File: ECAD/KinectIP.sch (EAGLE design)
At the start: 12 parts, among them P5+ 2PIN-FEMALE-HEADER

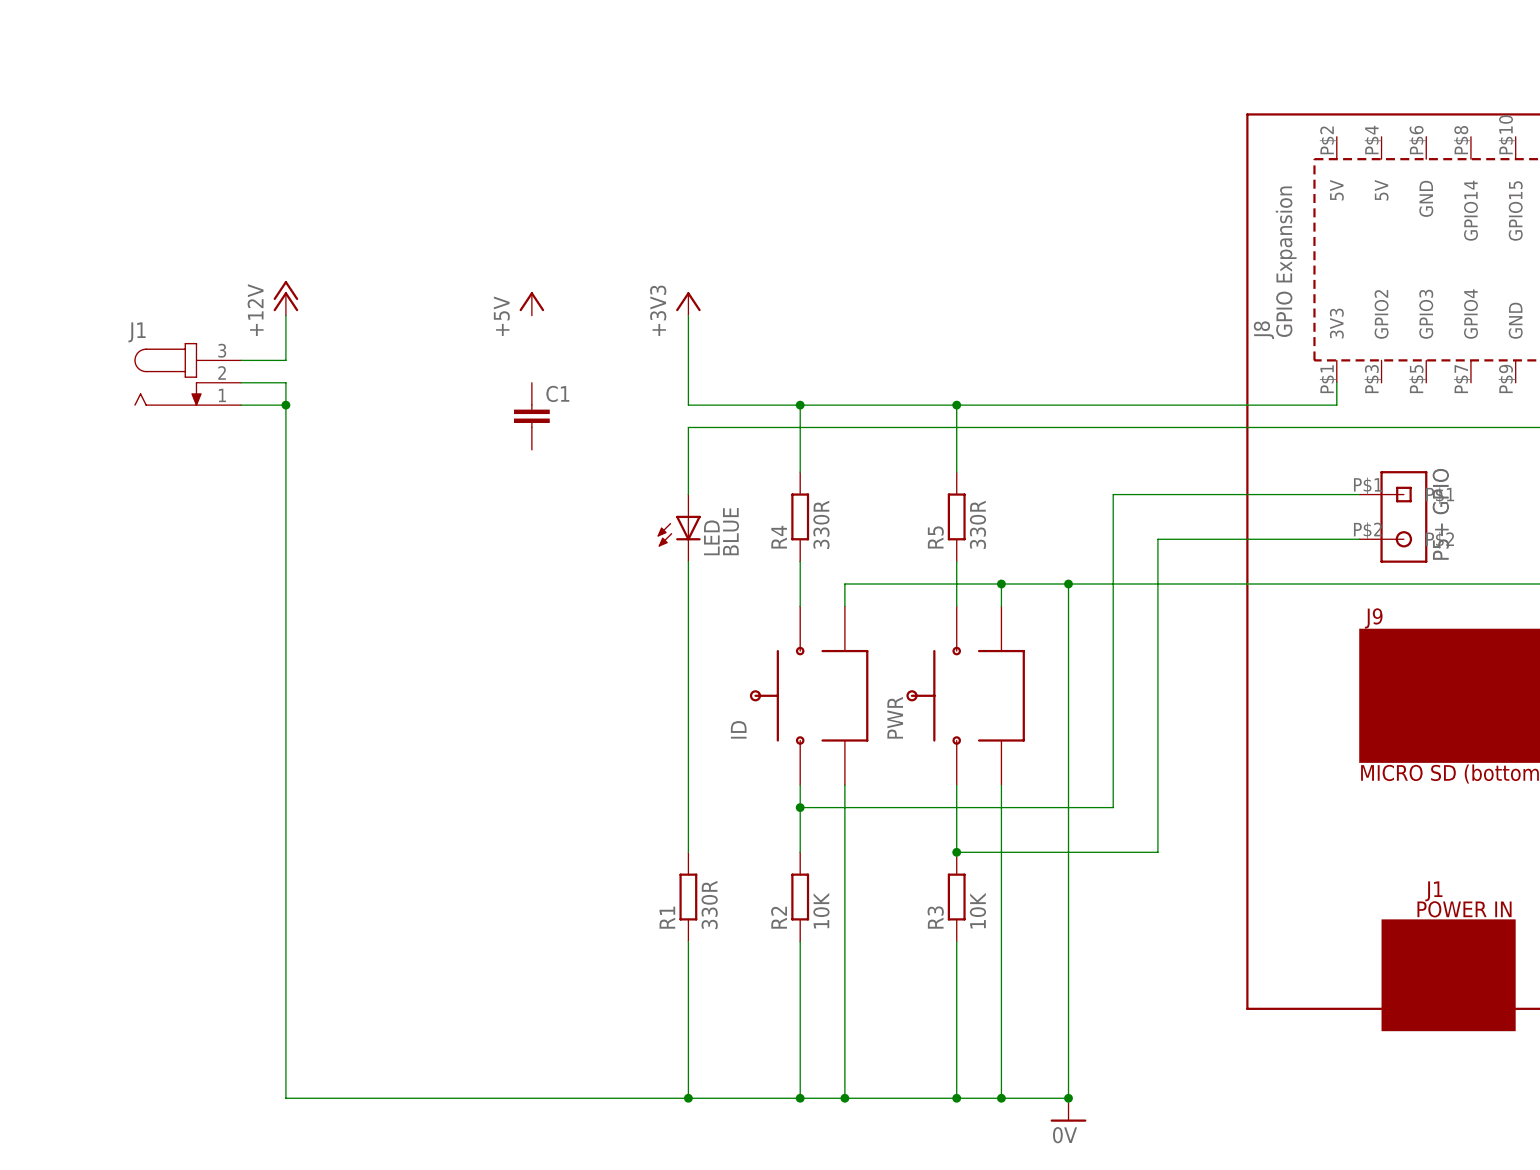
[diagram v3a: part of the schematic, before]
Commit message: add MP1584
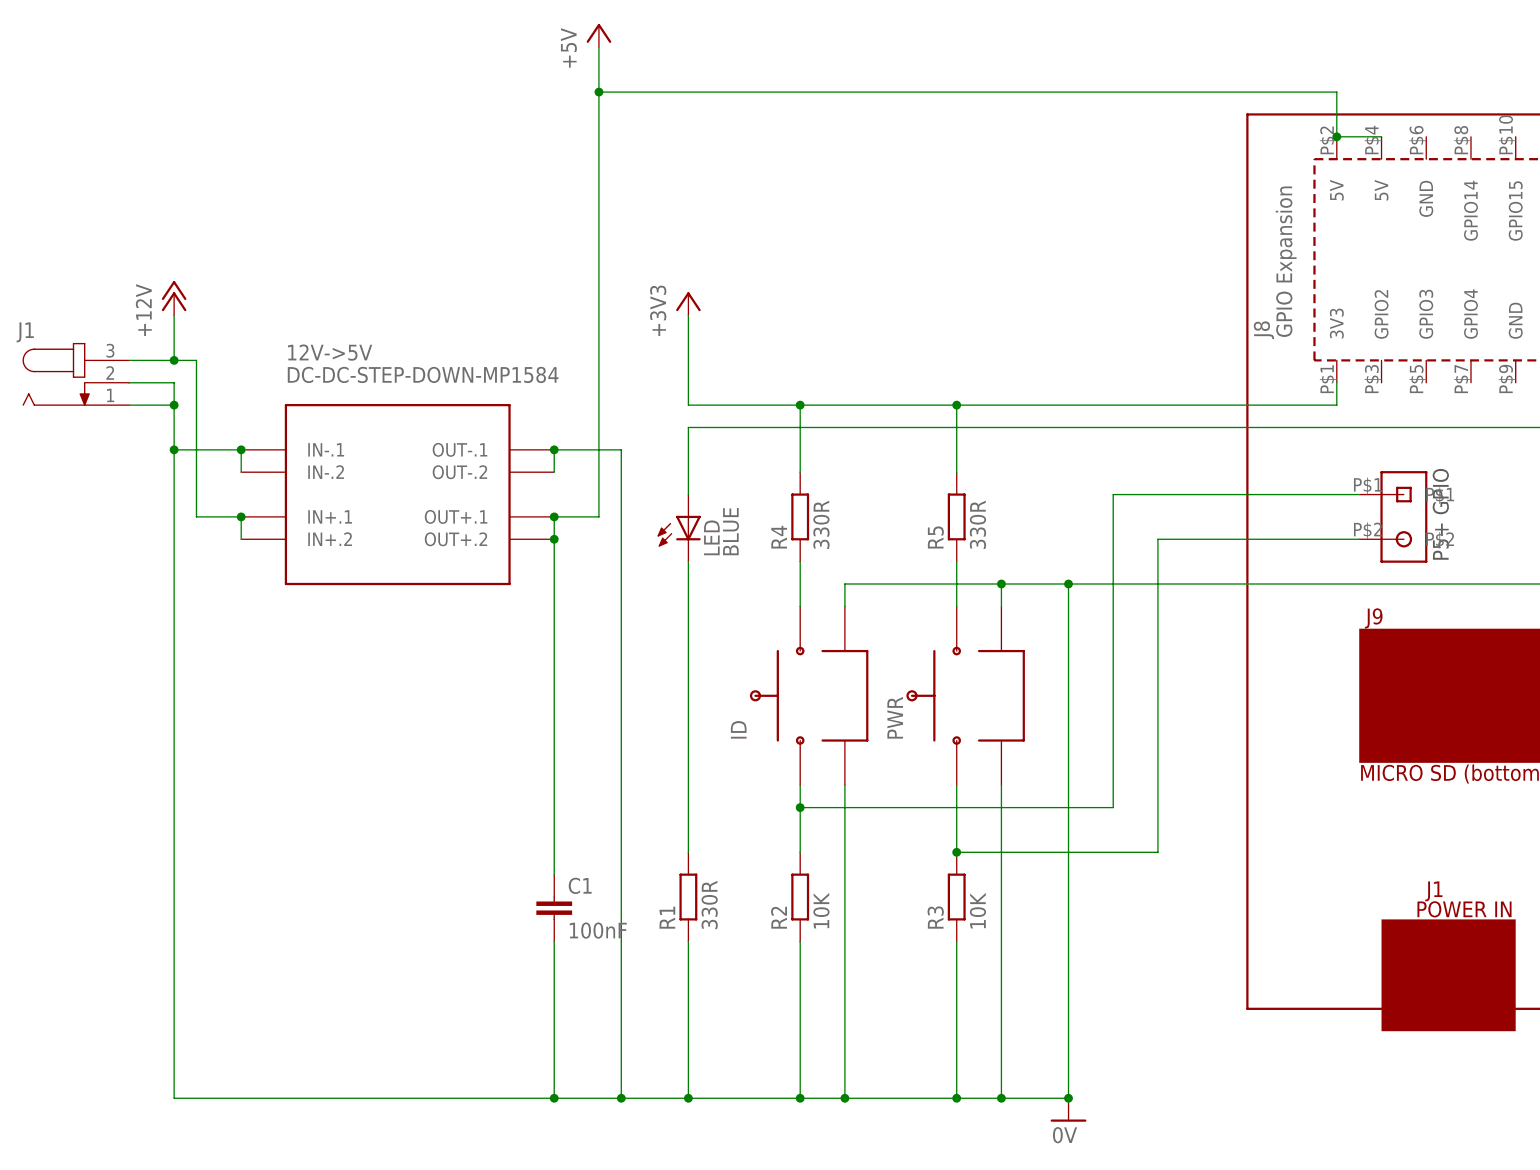
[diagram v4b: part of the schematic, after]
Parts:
- added 12V->5V: DC-DC-STEP-DOWN-MP1584, diy-modules:DC-DC-STEP-DOWN-MP1584
- C1: value (none) -> 100nF
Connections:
- new net +5V: 12V->5V.OUT+.1, 12V->5V.OUT+.2, C1.1, PCB2.5V@2, PCB2.5V@4
- net +12V: now also 12V->5V.IN+.1, 12V->5V.IN+.2
- net 0V: now also 12V->5V.IN-.1, 12V->5V.IN-.2, 12V->5V.OUT-.1, 12V->5V.OUT-.2, C1.2
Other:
- moved on the sheet: C1, J1
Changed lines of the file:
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@@
 <part name="J1" library="con-jack-3D" library_urn="urn:adsk.eagle:library:12345140" deviceset="JACK-PLUG-SLOTTED" device="0" package3d_urn="urn:adsk.eagle:package:12345148/2"/>
 <part name="LED" library="LED-90-Degree" library_urn="urn:adsk.eagle:library:12346089" deviceset="LED-90-DEG" device="" package3d_urn="urn:adsk.eagle:package:12346092/4" value="BLUE"/>
-<part name="C1" library="rcl" library_urn="urn:adsk.eagle:library:334" deviceset="C-EU" device="C0805K" package3d_urn="urn:adsk.eagle:package:23681/2"/>
+<part name="C1" library="rcl" library_urn="urn:adsk.eagle:library:334" deviceset="C-EU" device="C0805K" package3d_urn="urn:adsk.eagle:package:23681/2" value="100nF"/>
+<part name="12V-&gt;5V" library="diy-modules" library_urn="urn:adsk.eagle:library:12361804" deviceset="DC-DC-STEP-DOWN-MP1584" device="" package3d_urn="urn:adsk.eagle:package:12362133/2"/>
 </parts>
 <sheets>
@@
 <attribute name="VALUE" x="175.895" y="66.04" size="1.778" layer="96"/>
 </instance>
-<instance part="P+1" gate="1" x="116.84" y="162.56" smashed="yes">
-<attribute name="VALUE" x="114.3" y="157.48" size="1.778" layer="96" rot="R90"/>
-</instance>
-<instance part="P+2" gate="1" x="88.9" y="162.56" smashed="yes">
-<attribute name="VALUE" x="86.36" y="157.48" size="1.778" layer="96" rot="R90"/>
+<instance part="P+1" gate="1" x="124.46" y="193.04" smashed="yes">
+<attribute name="VALUE" x="121.92" y="187.96" size="1.778" layer="96" rot="R90"/>
+</instance>
+<instance part="P+2" gate="1" x="76.2" y="162.56" smashed="yes">
+<attribute name="VALUE" x="73.66" y="157.48" size="1.778" layer="96" rot="R90"/>
 </instance>
 <instance part="R4" gate="G$1" x="147.32" y="137.16" smashed="yes" rot="R90">
@@
 <attribute name="VALUE" x="168.402" y="133.35" size="1.778" layer="96" rot="R90"/>
 </instance>
-<instance part="J1" gate="G$1" x="78.74" y="152.4" smashed="yes">
-<attribute name="NAME" x="71.12" y="157.48" size="1.778" layer="95"/>
-<attribute name="VALUE" x="71.12" y="147.32" size="1.778" layer="96"/>
+<instance part="J1" gate="G$1" x="66.04" y="152.4" smashed="yes">
+<attribute name="NAME" x="58.42" y="157.48" size="1.778" layer="95"/>
+<attribute name="VALUE" x="58.42" y="147.32" size="1.778" layer="96"/>
 </instance>
 <instance part="LED" gate="G$1" x="134.62" y="134.62" smashed="yes">
@@
 <attribute name="VALUE" x="140.335" y="132.588" size="1.778" layer="96" rot="R90"/>
 </instance>
-<instance part="C1" gate="G$1" x="116.84" y="149.86" smashed="yes">
-<attribute name="NAME" x="118.364" y="150.241" size="1.778" layer="95"/>
-<attribute name="VALUE" x="118.364" y="145.161" size="1.778" layer="96"/>
+<instance part="C1" gate="G$1" x="119.38" y="93.98" smashed="yes">
+<attribute name="NAME" x="120.904" y="94.361" size="1.778" layer="95"/>
+<attribute name="VALUE" x="120.904" y="89.281" size="1.778" layer="96"/>
+</instance>
+<instance part="12V-&gt;5V" gate="G$1" x="101.6" y="139.7" smashed="yes">
+<attribute name="NAME" x="88.9" y="154.94" size="1.778" layer="95"/>
+<attribute name="VALUE" x="88.9" y="152.4" size="1.778" layer="96"/>
 </instance>
 </instances>
@@
 <wire x1="269.24" y1="129.54" x2="269.24" y2="152.4" width="0.1524" layer="91"/>
 <pinref part="J1" gate="G$1" pin="1"/>
-<wire x1="83.82" y1="149.86" x2="88.9" y2="149.86" width="0.1524" layer="91"/>
-<wire x1="88.9" y1="149.86" x2="88.9" y2="71.12" width="0.1524" layer="91"/>
-<wire x1="88.9" y1="71.12" x2="134.62" y2="71.12" width="0.1524" layer="91"/>
+<wire x1="71.12" y1="149.86" x2="76.2" y2="149.86" width="0.1524" layer="91"/>
+<wire x1="76.2" y1="149.86" x2="76.2" y2="144.78" width="0.1524" layer="91"/>
+<wire x1="76.2" y1="144.78" x2="76.2" y2="71.12" width="0.1524" layer="91"/>
+<wire x1="76.2" y1="71.12" x2="119.38" y2="71.12" width="0.1524" layer="91"/>
 <junction x="134.62" y="71.12"/>
 <pinref part="J1" gate="G$1" pin="2"/>
-<wire x1="83.82" y1="152.4" x2="88.9" y2="152.4" width="0.1524" layer="91"/>
-<wire x1="88.9" y1="152.4" x2="88.9" y2="149.86" width="0.1524" layer="91"/>
-<junction x="88.9" y="149.86"/>
+<wire x1="119.38" y1="71.12" x2="127" y2="71.12" width="0.1524" layer="91"/>
+<wire x1="127" y1="71.12" x2="134.62" y2="71.12" width="0.1524" layer="91"/>
+<wire x1="71.12" y1="152.4" x2="76.2" y2="152.4" width="0.1524" layer="91"/>
+<wire x1="76.2" y1="152.4" x2="76.2" y2="149.86" width="0.1524" layer="91"/>
+<junction x="76.2" y="149.86"/>
+<pinref part="12V-&gt;5V" gate="G$1" pin="IN-.1"/>
+<pinref part="12V-&gt;5V" gate="G$1" pin="IN-.2"/>
+<wire x1="83.82" y1="144.78" x2="83.82" y2="142.24" width="0.1524" layer="91"/>
+<wire x1="83.82" y1="144.78" x2="76.2" y2="144.78" width="0.1524" layer="91"/>
+<junction x="83.82" y="144.78"/>
+<junction x="76.2" y="144.78"/>
+<pinref part="12V-&gt;5V" gate="G$1" pin="OUT-.1"/>
+<pinref part="12V-&gt;5V" gate="G$1" pin="OUT-.2"/>
+<wire x1="119.38" y1="144.78" x2="119.38" y2="142.24" width="0.1524" layer="91"/>
+<wire x1="119.38" y1="144.78" x2="127" y2="144.78" width="0.1524" layer="91"/>
+<junction x="119.38" y="144.78"/>
+<wire x1="127" y1="144.78" x2="127" y2="71.12" width="0.1524" layer="91"/>
+<junction x="127" y="71.12"/>
+<pinref part="C1" gate="G$1" pin="2"/>
+<wire x1="119.38" y1="88.9" x2="119.38" y2="71.12" width="0.1524" layer="91"/>
+<junction x="119.38" y="71.12"/>
 </segment>
 </net>
@@
 <pinref part="J1" gate="G$1" pin="3"/>
 <pinref part="P+2" gate="1" pin="+12V"/>
-<wire x1="83.82" y1="154.94" x2="88.9" y2="154.94" width="0.1524" layer="91"/>
-<wire x1="88.9" y1="154.94" x2="88.9" y2="160.02" width="0.1524" layer="91"/>
-</segment>
-</net>
+<wire x1="71.12" y1="154.94" x2="76.2" y2="154.94" width="0.1524" layer="91"/>
+<wire x1="76.2" y1="154.94" x2="76.2" y2="160.02" width="0.1524" layer="91"/>
+<pinref part="12V-&gt;5V" gate="G$1" pin="IN+.1"/>
+<wire x1="83.82" y1="137.16" x2="78.74" y2="137.16" width="0.1524" layer="91"/>
+<wire x1="78.74" y1="137.16" x2="78.74" y2="154.94" width="0.1524" layer="91"/>
+<wire x1="78.74" y1="154.94" x2="76.2" y2="154.94" width="0.1524" layer="91"/>
+<junction x="76.2" y="154.94"/>
+<pinref part="12V-&gt;5V" gate="G$1" pin="IN+.2"/>
+<wire x1="83.82" y1="134.62" x2="83.82" y2="137.16" width="0.1524" layer="91"/>
+<junction x="83.82" y="137.16"/>
+</segment>
+</net>
+<net name="+5V" class="0">
+<segment>
+<pinref part="12V-&gt;5V" gate="G$1" pin="OUT+.1"/>
+<wire x1="124.46" y1="137.16" x2="119.38" y2="137.16" width="0.1524" layer="91"/>
+<pinref part="12V-&gt;5V" gate="G$1" pin="OUT+.2"/>
+<wire x1="119.38" y1="137.16" x2="119.38" y2="134.62" width="0.1524" layer="91"/>
+<junction x="119.38" y="137.16"/>
+<pinref part="C1" gate="G$1" pin="1"/>
+<wire x1="119.38" y1="96.52" x2="119.38" y2="134.62" width="0.1524" layer="91"/>
+<junction x="119.38" y="134.62"/>
+<pinref part="P+1" gate="1" pin="+5V"/>
+<wire x1="124.46" y1="137.16" x2="124.46" y2="185.42" width="0.1524" layer="91"/>
+<pinref part="PCB2" gate="G$1" pin="5V@2"/>
+<pinref part="PCB2" gate="G$1" pin="5V@4"/>
+<wire x1="124.46" y1="185.42" x2="124.46" y2="190.5" width="0.1524" layer="91"/>
+<wire x1="213.36" y1="180.34" x2="208.28" y2="180.34" width="0.1524" layer="91"/>
+<wire x1="208.28" y1="180.34" x2="208.28" y2="185.42" width="0.1524" layer="91"/>
+<wire x1="208.28" y1="185.42" x2="124.46" y2="185.42" width="0.1524" layer="91"/>
+<junction x="208.28" y="180.34"/>
+<junction x="124.46" y="185.42"/>
+</segment>
+</net>
